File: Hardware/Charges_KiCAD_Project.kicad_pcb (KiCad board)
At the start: 4 copper layers, 80 x 93.5 mm, 38 parts, among them IC1 TP124005-2, IC2 STM32L562VET6Q, J1 796684-4, J2 796684-4, J3 D37S13A4GX00LF, Q1 SI7232DN-T1-GE3, Q2 SI7232DN-T1-GE3, U1 MS5607-02BA, Y1 32mhz

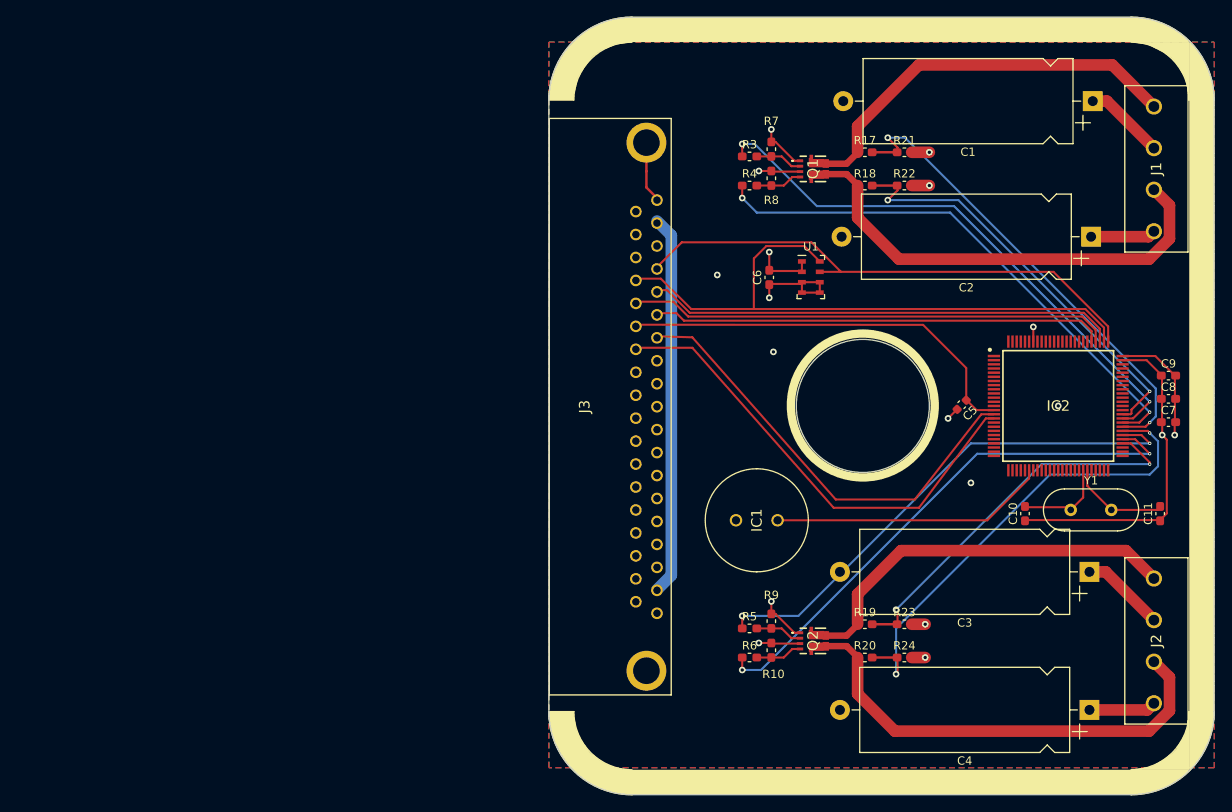
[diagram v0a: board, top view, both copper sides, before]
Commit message: Added correct crystal for mcu, re-routing of data lines in progress
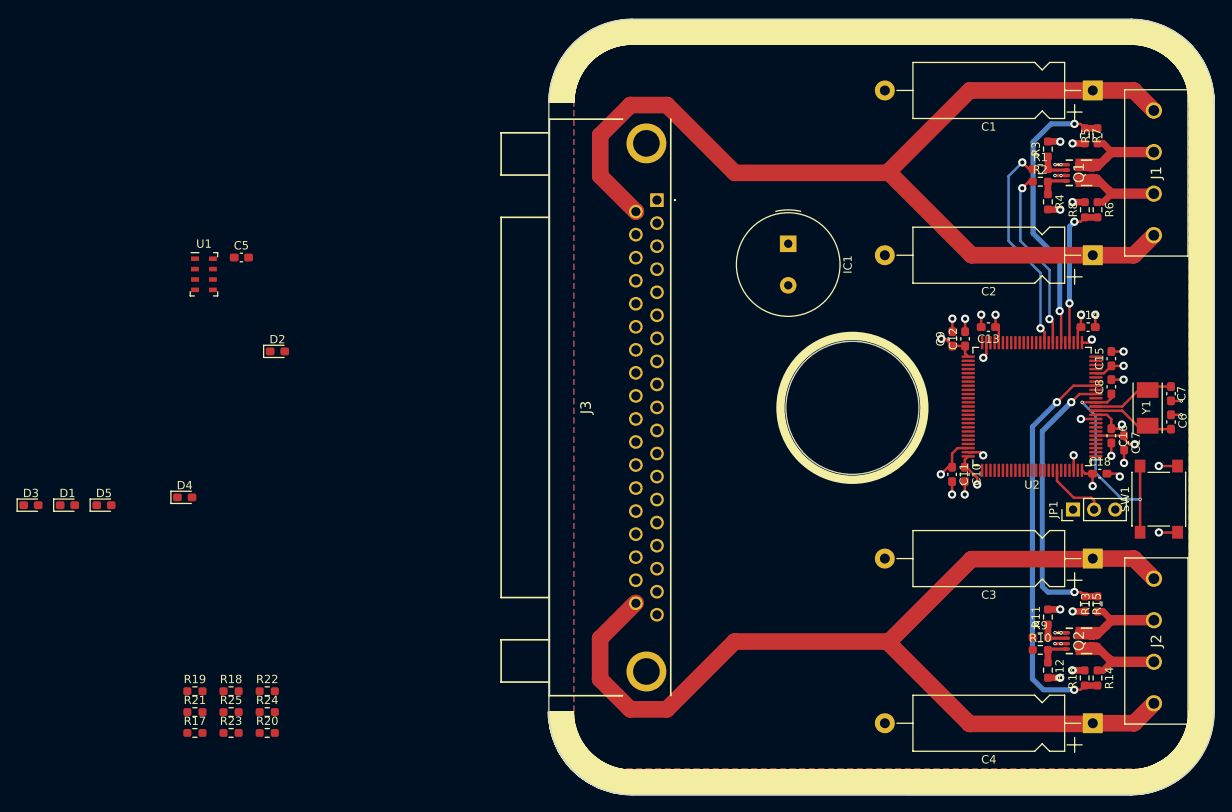
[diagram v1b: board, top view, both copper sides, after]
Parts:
- removed IC2: STM32L562VET6Q, SamacSys_Parts:QFP50P1600X1600X160-100N
- added C12: 100nF, Capacitor_SMD:C_0603_1608Metric_Pad1.08x0.95mm_HandSolder, F.Cu at (138.6, 88.2)
- added C13: 100nF, Capacitor_SMD:C_0603_1608Metric_Pad1.08x0.95mm_HandSolder, F.Cu at (141.3, 86.8)
- added C14: 100nF, Capacitor_SMD:C_0603_1608Metric_Pad1.08x0.95mm_HandSolder, F.Cu at (153.3, 86.8)
- added C15: 100nF, Capacitor_SMD:C_0603_1608Metric_Pad1.08x0.95mm_HandSolder, F.Cu at (156.1, 90.6)
- added C16: 100nF, Capacitor_SMD:C_0603_1608Metric_Pad1.08x0.95mm_HandSolder, F.Cu at (156.1, 99.8)
- added C17: 100nF, Capacitor_SMD:C_0603_1608Metric_Pad1.08x0.95mm_HandSolder, F.Cu at (157.7, 100.7)
- added C18: 100nF, Capacitor_SMD:C_0603_1608Metric_Pad1.08x0.95mm_HandSolder, F.Cu at (154.7, 104.4)
- added D1: Red, LED_SMD:LED_0603_1608Metric_Pad1.05x0.95mm_HandSolder, F.Cu at (30.6, 108.2)
- added D2: Grn, LED_SMD:LED_0603_1608Metric_Pad1.05x0.95mm_HandSolder, F.Cu at (55.9, 89.7)
- added D3: Red, LED_SMD:LED_0603_1608Metric_Pad1.05x0.95mm_HandSolder, F.Cu at (26.2, 108.2)
- added D4: Grn, LED_SMD:LED_0603_1608Metric_Pad1.05x0.95mm_HandSolder, F.Cu at (44.7, 107.2)
- added D5: Red, LED_SMD:LED_0603_1608Metric_Pad1.05x0.95mm_HandSolder, F.Cu at (35.0, 108.2)
- added JP1: Debug Jumper, Connector_PinHeader_2.54mm:PinHeader_1x03_P2.54mm_Vertical, F.Cu at (151.5, 108.7)
- added R1: 1k, Resistor_SMD:R_0603_1608Metric_Pad0.98x0.95mm_HandSolder, F.Cu at (147.6, 67.8)
- added R11: 10k, Resistor_SMD:R_0603_1608Metric_Pad0.98x0.95mm_HandSolder, F.Cu at (148.5, 121.6)
- added R12: 10k, Resistor_SMD:R_0603_1608Metric_Pad0.98x0.95mm_HandSolder, F.Cu at (148.5, 128.0)
- added R13: 100k, Resistor_SMD:R_0603_1608Metric_Pad0.98x0.95mm_HandSolder, F.Cu at (154.5, 120.1)
- added R14: 100k, Resistor_SMD:R_0603_1608Metric_Pad0.98x0.95mm_HandSolder, F.Cu at (154.5, 129.0)
- added R15: 27k, Resistor_SMD:R_0603_1608Metric_Pad0.98x0.95mm_HandSolder, F.Cu at (153.0, 120.1)
- added R16: 27k, Resistor_SMD:R_0603_1608Metric_Pad0.98x0.95mm_HandSolder, F.Cu at (152.9, 129.0)
- added R2: 1k, Resistor_SMD:R_0603_1608Metric_Pad0.98x0.95mm_HandSolder, F.Cu at (147.6, 69.3)
- added R25: 4.7k, Resistor_SMD:R_0603_1608Metric_Pad0.98x0.95mm_HandSolder, F.Cu at (50.3, 133.1)
- added SW1: MCU Reset, Button_Switch_SMD:SW_SPST_PTS645, F.Cu at (161.8, 107.5)
- added U2: STM32L562VET6Q, Package_QFP:LQFP-100_14x14mm_P0.5mm, F.Cu at (146.6, 96.3)
- C1, C2, C3, C4: value CP1_Small -> 1500uF; footprint Capacitor_THT:CP_Axial_L25.0mm_D10.0mm_P30.00mm_Horizontal -> Capacitor_THT:CP_Axial_L18.0mm_D6.5mm_P25.00mm_Horizontal
- C10, C11: value 30pF -> 100nF
- C5: footprint Capacitor_SMD:C_0603_1608Metric -> Capacitor_SMD:C_0603_1608Metric_Pad1.08x0.95mm_HandSolder
- C6: value 100nF -> 30pF
- C7: value 1uF -> 30pF
- C9: value 100nF -> 1uF
- IC1: footprint SamacSys_Parts:TP1240052 -> Buzzer_Beeper:Buzzer_TDK_PS1240P02BT_D12.2mm_H6.5mm
- J1, J2: value 796684-4 -> Terminal Block
- J3: value D37S13A4GX00LF -> DB37_Male_MountingHoles; footprint SamacSys_Parts:D37S13A4GX00LF -> RDT_Custom_Footprints:L717SDC37P1ACH4F
- R10, R9: value 10k -> 1k; footprint Resistor_SMD:R_0603_1608Metric_Pad1.05x0.95mm_HandSolder -> Resistor_SMD:R_0603_1608Metric_Pad0.98x0.95mm_HandSolder
- R17, R18, R19, R20: value 100k -> 820; footprint Resistor_SMD:R_0603_1608Metric_Pad1.05x0.95mm_HandSolder -> Resistor_SMD:R_0603_1608Metric_Pad0.98x0.95mm_HandSolder
- R21: value 27k -> 820; footprint Resistor_SMD:R_0603_1608Metric_Pad1.05x0.95mm_HandSolder -> Resistor_SMD:R_0603_1608Metric_Pad0.98x0.95mm_HandSolder
- R22, R23, R24: value 27k -> 4.7k; footprint Resistor_SMD:R_0603_1608Metric_Pad1.05x0.95mm_HandSolder -> Resistor_SMD:R_0603_1608Metric_Pad0.98x0.95mm_HandSolder
- R3, R4: value 1k -> 10k; footprint Resistor_SMD:R_0603_1608Metric_Pad1.05x0.95mm_HandSolder -> Resistor_SMD:R_0603_1608Metric_Pad0.98x0.95mm_HandSolder
- R5, R6: value 1k -> 100k; footprint Resistor_SMD:R_0603_1608Metric_Pad1.05x0.95mm_HandSolder -> Resistor_SMD:R_0603_1608Metric_Pad0.98x0.95mm_HandSolder
- R7, R8: value 10k -> 27k; footprint Resistor_SMD:R_0603_1608Metric_Pad1.05x0.95mm_HandSolder -> Resistor_SMD:R_0603_1608Metric_Pad0.98x0.95mm_HandSolder
- Y1: value 32mhz -> 32MHz; footprint Crystal:Crystal_HC49-4H_Vertical -> RDT_Custom_Footprints:XTAL_ABM7-32.000MHZ-D2Y-T
- moved R21 108.7 mm to (45.9, 133.1)
- moved R17 106.6 mm to (45.9, 135.6)
- moved R22 97.8 mm to (54.6, 130.6)
- moved R18 97.5 mm to (50.3, 130.6)
- moved C5 88.4 mm to (51.5, 78.4), turned to 0 degrees
- moved R23 82.0 mm to (50.3, 135.6)
- moved R19 81.0 mm to (45.9, 130.6)
- moved R24 76.9 mm to (54.6, 133.1)
- moved U1 73.0 mm to (47.0, 80.4)
- moved R5 72.5 mm to (154.5, 63.8), turned to 90 degrees
- moved R20 72.4 mm to (54.6, 135.6)
- moved R6 68.2 mm to (154.5, 72.7), turned to -90 degrees
- moved C6 51.3 mm to (163.3, 98.2)
- moved R8 37.9 mm to (153.0, 72.7)
- moved R7 37.7 mm to (153.0, 63.8), turned to -90 degrees
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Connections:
- net /DSUB_37_Male/t_clk renamed /37 Pin DSUB/t_clk
- net /DSUB_37_Male/t_miso renamed /37 Pin DSUB/t_miso
- net /DSUB_37_Male/t_mosi renamed /37 Pin DSUB/t_mosi
- C10 pad 1: GND -> +3V3
- C10 pad 2: Net-(C10-Pad2) -> GND
- C11 pad 1: GND -> +3V3
- C11 pad 2: Net-(C11-Pad2) -> GND
- C5 pad 1: /NRST -> GND
- C5 pad 2: GND -> +3V3
- C6 pad 1: GND -> Net-(C6-Pad1)
- C6 pad 2: +3V3 -> GND
- C7 pad 1: GND -> Net-(C7-Pad1)
- C7 pad 2: +3V3 -> GND
- C8 pad 1: GND -> /37 Pin DSUB/NRST
- C8 pad 2: +3V3 -> GND
- C9 pad 1: GND -> +3V3
- C9 pad 2: +3V3 -> GND
- IC1 pad 1: /Buzzer_Excitation -> /MCU L562VET6Q/Buzzer
- J1 pad 1: /Fet_A -> +5V
- J1 pad 2: +5V -> /Igniter A
- J1 pad 3: /Fet_B -> /Igniter B
- J2 pad 1: /Fet_C -> +5V
- J2 pad 2: +5V -> /Igniter C
- J2 pad 3: /Fet_D -> /Igniter D
- J3 pad 23: /SWCLK -> /37 Pin DSUB/SWCLK
- J3 pad 24: /Alert_sda -> /37 Pin DSUB/Alert_sda
- J3 pad 25: /NRST -> /37 Pin DSUB/NRST
- J3 pad 26: /Fire_Redundant -> /37 Pin DSUB/Fire_redundant
- J3 pad 4: /SWDIO -> /37 Pin DSUB/SWDIO
- J3 pad 5: /Alert_scl -> /37 Pin DSUB/Alert_scl
- J3 pad 6: /Alert_Active -> /37 Pin DSUB/Alert_Active
- J3 pad 7: /Fire -> /37 Pin DSUB/Fire
- J3 pad MH1: GND -> (no net)
- J3 pad MH2: GND -> (no net)
- Q1 pad 10: /Fet_A -> /Igniter A
- Q1 pad 11: /Fet_A -> /Igniter A
- Q1 pad 12: /Fet_B -> /Igniter B
- Q1 pad 13: /Fet_B -> /Igniter B
- Q1 pad 14: /Fet_B -> /Igniter B
- Q1 pad 15: /Fet_A -> /Igniter A
- Q1 pad 16: /Fet_B -> /Igniter B
- Q1 pad 5: /Fet_B -> /Igniter B
- Q1 pad 6: /Fet_B -> /Igniter B
- Q1 pad 7: /Fet_A -> /Igniter A
- Q1 pad 8: /Fet_A -> /Igniter A
- Q1 pad 9: /Fet_A -> /Igniter A
- Q2 pad 10: /Fet_C -> /Igniter C
- Q2 pad 11: /Fet_C -> /Igniter C
- Q2 pad 12: /Fet_D -> /Igniter D
- Q2 pad 13: /Fet_D -> /Igniter D
- Q2 pad 14: /Fet_D -> /Igniter D
- Q2 pad 15: /Fet_C -> /Igniter C
- Q2 pad 16: /Fet_D -> /Igniter D
- Q2 pad 5: /Fet_D -> /Igniter D
- Q2 pad 6: /Fet_D -> /Igniter D
- Q2 pad 7: /Fet_C -> /Igniter C
- Q2 pad 8: /Fet_C -> /Igniter C
- Q2 pad 9: /Fet_C -> /Igniter C
- R10 pad 1: Net-(Q2-Pad4) -> /Fire_D
- R10 pad 2: GND -> Net-(Q2-Pad4)
- R17 pad 1: /Fet_A -> GND
- R17 pad 2: /Sense_A -> Net-(D1-Pad1)
- R18 pad 1: /Fet_B -> GND
- R18 pad 2: /Sense_B -> Net-(D2-Pad1)
- R19 pad 1: /Fet_C -> GND
- R19 pad 2: /Sense_C -> Net-(D3-Pad1)
- R20 pad 1: /Fet_D -> GND
- R20 pad 2: /Sense_D -> Net-(D4-Pad1)
- R21 pad 1: /Sense_A -> GND
- R21 pad 2: GND -> Net-(D5-Pad1)
- R22 pad 1: /Sense_B -> /37 Pin DSUB/Alert_scl
- R22 pad 2: GND -> +3V3
- R23 pad 1: /Sense_C -> /37 Pin DSUB/Alert_sda
- R23 pad 2: GND -> +3V3
- R24 pad 1: /Sense_D -> /Barometer_MS5607/SCLK
- R24 pad 2: GND -> +3V3
- R3 pad 1: /Fire_A -> Net-(Q1-Pad2)
- R3 pad 2: Net-(Q1-Pad2) -> GND
- R4 pad 1: /Fire_B -> Net-(Q1-Pad4)
- R4 pad 2: Net-(Q1-Pad4) -> GND
- R5 pad 1: /Fire_C -> /Igniter A
- R5 pad 2: Net-(Q2-Pad2) -> /Sense_A
- R6 pad 1: /Fire_D -> /Igniter B
- R6 pad 2: Net-(Q2-Pad4) -> /Sense_B
- R7 pad 1: Net-(Q1-Pad2) -> /Sense_A
- R8 pad 1: Net-(Q1-Pad4) -> /Sense_B
- R9 pad 1: Net-(Q2-Pad2) -> /Fire_C
- R9 pad 2: GND -> Net-(Q2-Pad2)
- U1 pad 6: GND -> /Barometer_MS5607/SDO
- U1 pad 7: /SWDIO -> /Barometer_MS5607/SDI_SDA
- U1 pad 8: /SWCLK -> /Barometer_MS5607/SCLK
- Y1 pad 1: Net-(C10-Pad2) -> Net-(C6-Pad1)
- Y1 pad 2: Net-(C11-Pad2) -> Net-(C7-Pad1)
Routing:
- net +5V: track 35.7 -> 248.8 mm
- net +3V3: track 153.6 -> 38.7 mm, vias 2 -> 9
- net /SWCLK: track 75.8 -> 0.00 mm
- net /Fire_D: track 65.3 -> 0.00 mm, vias 2 -> 0
- net /SWDIO: track 64.0 -> 0.00 mm
- net /Fire_C: track 62.8 -> 0.00 mm, vias 2 -> 0
- net /Alert_sda: track 58.1 -> 0.00 mm
- net /Fire_Redundant: track 57.1 -> 0.00 mm
- net /Alert_scl: track 56.7 -> 0.00 mm
- net /Fet_D: track 56.4 -> 0.00 mm
- net /Fet_B: track 56.1 -> 0.00 mm
- net /Alert_Active: track 54.4 -> 0.00 mm
- net /Fire: track 54.3 -> 0.00 mm
- net /NRST: track 49.6 -> 0.00 mm
- net /Fet_A: track 48.9 -> 0.00 mm
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- added copper zone on In2.Cu, net +3V3
- removed copper zone on In2.Cu, net +5V
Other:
- board size 80 x 93.5 mm -> 80 x 93.2 mm

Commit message: Routed Alert I2C lines
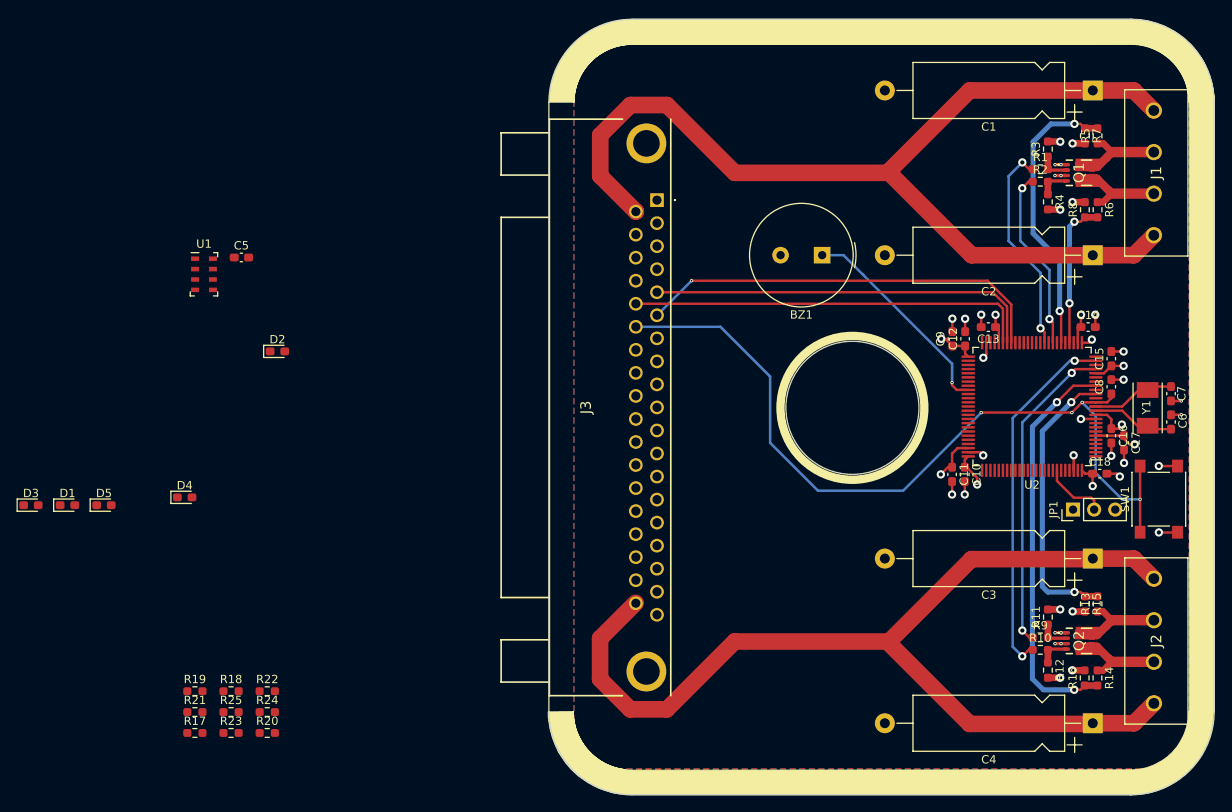
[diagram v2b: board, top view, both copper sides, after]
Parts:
- moved BZ1 4.30 mm to (121.4, 78.1), turned to 180 degrees
- renumbered IC1 to BZ1
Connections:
- R22 pad 1: /37 Pin DSUB/Alert_scl -> /Barometer_MS5607/SCLK
- R23 pad 1: /37 Pin DSUB/Alert_sda -> /Barometer_MS5607/SDI_SDA
- R24 pad 1: /Barometer_MS5607/SCLK -> /37 Pin DSUB/Alert_scl
- R25 pad 1: /Barometer_MS5607/SDI_SDA -> /37 Pin DSUB/Alert_sda
- U2 pad 43: unconnected-(U2-Pad43) -> /37 Pin DSUB/Alert_Active
- U2 pad 44: /Barometer_MS5607/SCLK -> /37 Pin DSUB/Alert_scl
- U2 pad 45: /Barometer_MS5607/SDI_SDA -> /37 Pin DSUB/Alert_sda
- U2 pad 91: /37 Pin DSUB/Alert_Active -> /MCU L562VET6Q/I2C1_EN
- U2 pad 92: /37 Pin DSUB/Alert_scl -> /Barometer_MS5607/SCLK
- U2 pad 93: /37 Pin DSUB/Alert_sda -> /Barometer_MS5607/SDI_SDA
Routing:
- net /37 Pin DSUB/NRST: track 28.0 -> 98.9 mm, vias 2 -> 4
- net /37 Pin DSUB/Alert_Active: track 0.00 -> 50.1 mm, vias 0 -> 1
- net /37 Pin DSUB/Alert_sda: track 0.00 -> 48.5 mm
- net /37 Pin DSUB/Alert_scl: track 0.00 -> 47.2 mm
- net /Fire_D: track 0.00 -> 43.4 mm, vias 0 -> 2
- net /Fire_C: track 0.00 -> 38.1 mm, vias 0 -> 2
- net /MCU L562VET6Q/Buzzer: track 0.00 -> 25.8 mm, vias 0 -> 1

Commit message: Routed all traces and components, need to place LEDs
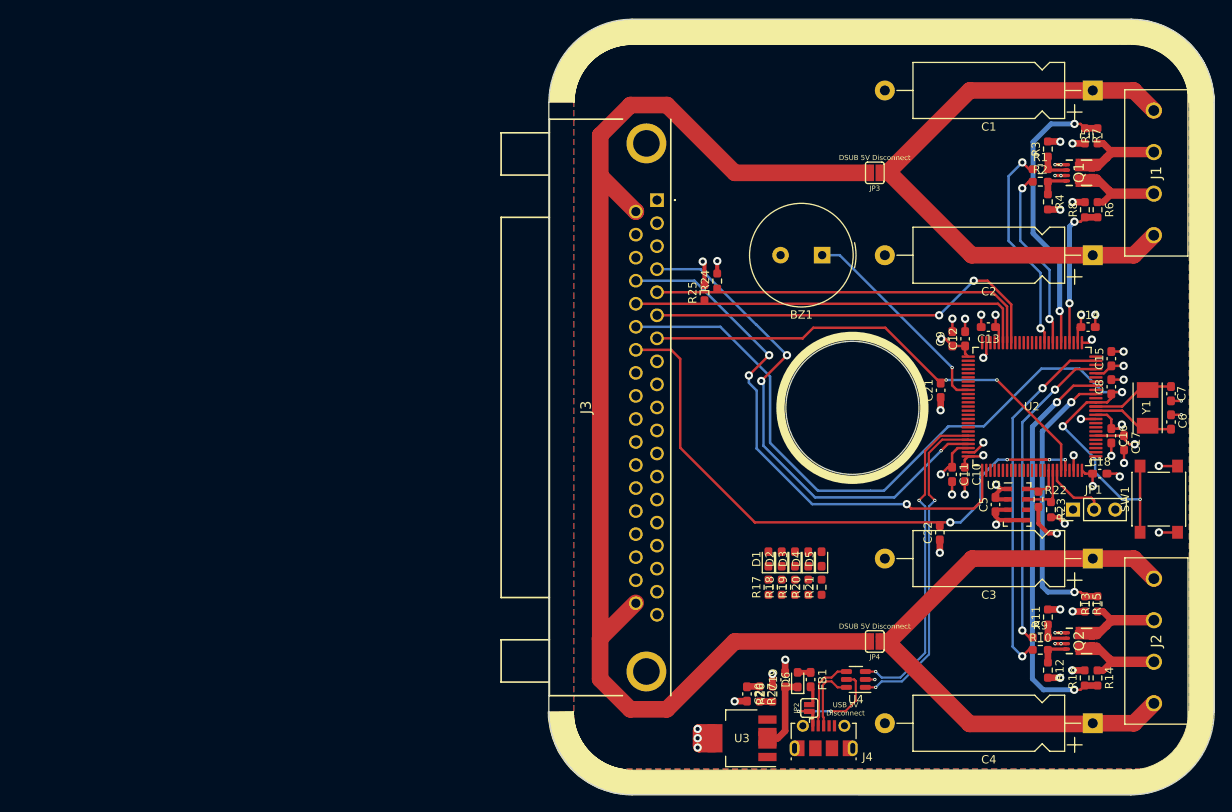
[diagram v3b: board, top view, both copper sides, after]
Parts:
- added C19: 0.1uF, Capacitor_SMD:C_0603_1608Metric_Pad1.08x0.95mm_HandSolder, F.Cu at (116.9, 129.2)
- added C20: 1uF, Capacitor_SMD:C_0603_1608Metric_Pad1.08x0.95mm_HandSolder, F.Cu at (112.3, 130.9)
- added C21: 100nF, Capacitor_SMD:C_0603_1608Metric_Pad1.08x0.95mm_HandSolder, F.Cu at (135.6, 94.4)
- added C22: 100nF, Capacitor_SMD:C_0603_1608Metric_Pad1.08x0.95mm_HandSolder, F.Cu at (135.5, 111.5)
- added D6: D_Schottky_Small, Diode_SMD:D_0603_1608Metric_Pad1.05x0.95mm_HandSolder, F.Cu at (118.4, 129.2)
- added FB1: Ferrite_Bead_Small, Capacitor_SMD:C_0603_1608Metric_Pad1.08x0.95mm_HandSolder, F.Cu at (120.0, 129.2)
- added J4: 10118192-0001LF, Connector_USB:USB_Micro-B_Molex-105017-0001, F.Cu at (121.5, 136.2)
- added JP2: USB 5V Disconnect, Jumpers:SMT-JUMPER_2_NO_SILK, F.Cu at (119.8, 132.6)
- added JP3: DSUB 5V Disconnect, Jumpers:SMT-JUMPER_2_NO_SILK, F.Cu at (127.7, 68.2)
- added JP4: DSUB 5V Disconnect, Jumpers:SMT-JUMPER_2_NO_SILK, F.Cu at (127.7, 124.6)
- added R26: 390, Resistor_SMD:R_0603_1608Metric_Pad0.98x0.95mm_HandSolder, F.Cu at (115.4, 130.9)
- added R27: 240, Resistor_SMD:R_0603_1608Metric_Pad0.98x0.95mm_HandSolder, F.Cu at (113.8, 130.9)
- added U3: LP38692MPX-ADJ, Package_TO_SOT_SMD:SOT-223-5, F.Cu at (111.7, 136.2)
- added U4: USBLC6-2SC6, Package_TO_SOT_SMD:SOT-23-6, F.Cu at (125.4, 129.1)
- moved R23 102.2 mm to (148.9, 108.7), turned to -90 degrees
- moved U1 101.6 mm to (144.8, 108.1)
- moved R22 95.6 mm to (147.4, 107.5), turned to -90 degrees
- moved C5 95.4 mm to (142.2, 108.1), turned to 90 degrees
- moved D3 92.1 mm to (118.1, 114.7), turned to 90 degrees
- moved D5 86.5 mm to (121.3, 114.7), turned to 90 degrees
- moved D1 84.5 mm to (114.9, 114.6), turned to 90 degrees
- moved R21 76.8 mm to (121.3, 118.0), turned to 90 degrees
- moved R25 76.0 mm to (107.2, 82.6), turned to 90 degrees
- moved D4 75.3 mm to (119.7, 114.7), turned to 90 degrees
- moved R24 74.9 mm to (108.7, 81.2), turned to 90 degrees
- moved R19 73.2 mm to (118.1, 118.0), turned to 90 degrees
- moved R17 71.2 mm to (114.9, 118.0), turned to 90 degrees
- moved R18 67.4 mm to (116.5, 118.0), turned to 90 degrees
- moved R20 67.4 mm to (119.7, 118.0), turned to 90 degrees
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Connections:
- J3 pad 20: +5V -> /37 Pin DSUB/DSUB-5V
- J3 pad 37: +5V -> /37 Pin DSUB/DSUB-5V
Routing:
- net /37 Pin DSUB/DSUB-5V: track 0.00 -> 155.7 mm
- net +5V: track 248.8 -> 153.8 mm
- net /37 Pin DSUB/Fire_redundant: track 0.00 -> 73.1 mm, vias 0 -> 4
- net /37 Pin DSUB/SWCLK: track 0.00 -> 66.5 mm, vias 0 -> 3
- net /37 Pin DSUB/SWDIO: track 0.00 -> 61.6 mm, vias 0 -> 3
- net /37 Pin DSUB/Fire: track 0.00 -> 58.1 mm, vias 0 -> 2
- net /MCU L562VET6Q/USB_D-: track 0.00 -> 39.5 mm, vias 0 -> 2
- net /MCU L562VET6Q/USB_D+: track 0.00 -> 39.5 mm, vias 0 -> 2
- net +3V3: track 38.7 -> 63.4 mm, vias 9 -> 17
- net GND: track 51.5 -> 67.4 mm, vias 36 -> 43
- net Net-(C19-Pad1): track 0.00 -> 14.9 mm
- net /USB Connector and ESD/USB_5V: track 0.00 -> 14.1 mm, vias 0 -> 2
- net /37 Pin DSUB/NRST: track 98.9 -> 109.9 mm, vias 4 -> 3
- net /USB Connector and ESD/USB_CONN_D-: track 0.00 -> 9.03 mm
- net /USB Connector and ESD/USB_CONN_D+: track 0.00 -> 8.26 mm
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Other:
- board text added: "USB 5V Disconnect"

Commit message: All traces routed
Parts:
- moved R17 55.8 mm to (162.1, 88.2), turned to 180 degrees
- moved R18 55.4 mm to (162.1, 86.6), turned to 180 degrees
- moved R19 55.0 mm to (162.1, 85.0), turned to 180 degrees
- moved R20 54.7 mm to (162.1, 83.4), turned to 180 degrees
- moved R21 54.6 mm to (162.1, 81.8), turned to 180 degrees
- moved D1 51.2 mm to (158.7, 88.2), turned to 180 degrees
- moved D2 50.7 mm to (158.7, 86.6), turned to 180 degrees
- moved D3 50.3 mm to (158.7, 85.0), turned to 180 degrees
- moved D4 50.0 mm to (158.7, 83.4), turned to 180 degrees
- moved D5 49.8 mm to (158.7, 81.8), turned to 180 degrees
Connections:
- D1 pad 2: unconnected-(D1-Pad2) -> Net-(U2-Pad38)
- D2 pad 2: unconnected-(D2-Pad2) -> Net-(U2-Pad39)
- D3 pad 2: unconnected-(D3-Pad2) -> Net-(U2-Pad40)
- D4 pad 2: unconnected-(D4-Pad2) -> Net-(U2-Pad41)
- D5 pad 2: unconnected-(D5-Pad2) -> Net-(U2-Pad42)
- U2 pad 38: unconnected-(U2-Pad38) -> Net-(U2-Pad38)
- U2 pad 39: unconnected-(U2-Pad39) -> Net-(U2-Pad39)
- U2 pad 40: unconnected-(U2-Pad40) -> Net-(U2-Pad40)
- U2 pad 41: unconnected-(U2-Pad41) -> Net-(U2-Pad41)
- U2 pad 42: unconnected-(U2-Pad42) -> Net-(U2-Pad42)
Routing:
- net Net-(U2-Pad38): track 0.00 -> 19.0 mm
- net Net-(U2-Pad42): track 0.00 -> 18.8 mm
- net Net-(U2-Pad39): track 0.00 -> 18.7 mm
- net Net-(U2-Pad41): track 0.00 -> 18.4 mm
- net Net-(U2-Pad40): track 0.00 -> 18.0 mm
- net GND: track 67.4 -> 77.3 mm, vias 43 -> 49
- net Net-(R26-Pad1): track 1.53 -> 5.18 mm
- net /37 Pin DSUB/Fire_redundant: track 73.1 -> 74.9 mm
- net Net-(D1-Pad1): track 0.00 -> 1.61 mm
- net Net-(D5-Pad1): track 0.00 -> 1.61 mm
- net Net-(D4-Pad1): track 0.00 -> 1.61 mm
- net Net-(D3-Pad1): track 0.00 -> 1.61 mm
- net Net-(D2-Pad1): track 0.00 -> 1.61 mm
